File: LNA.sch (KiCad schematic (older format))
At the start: 81 parts, among them CN1 EPS.00.250.NTN, CN2 EPS.00.250.NTN, CN3 EPS.00.250.NTN, CN4 EPS.00.250.NTN, J5 TEST_1P, J6 TEST_1P, J7 TEST_1P, J8 TEST_1P, U1 AD8334ACPZ

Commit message: Bug fixed 1
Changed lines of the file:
@@
 $EndComp
 Connection ~ 5700 7300
-Wire Wire Line
-	5700 5400 5700 5500
 $Comp
 L +5V #PWR21
 U 1 1 599B21E3
-P 5650 5450
-F 0 "#PWR21" H 5650 5300 50  0001 C CNN
-F 1 "+5V" H 5650 5590 50  0000 C CNN
-F 2 "" H 5650 5450 50  0001 C CNN
-F 3 "" H 5650 5450 50  0001 C CNN
-	1    5650 5450
-	0    -1   -1   0
-$EndComp
-Connection ~ 5700 5450
+P 5600 5400
+F 0 "#PWR21" H 5600 5250 50  0001 C CNN
+F 1 "+5V" H 5600 5540 50  0000 C CNN
+F 2 "" H 5600 5400 50  0001 C CNN
+F 3 "" H 5600 5400 50  0001 C CNN
+	1    5600 5400
+	0    -1   -1   0
+$EndComp
 $Comp
 L C_Small C1
@@
 $EndComp
 Wire Wire Line
-	5700 5450 5650 5450
-Wire Wire Line
 	4800 5400 4800 5300
 Connection ~ 4800 5300
@@
 Wire Wire Line
 	1700 6100 1650 6100
+$Comp
+L GNDA #PWR?
+U 1 1 5AD964B4
+P 5550 5500
+F 0 "#PWR?" H 5550 5250 50  0001 C CNN
+F 1 "GNDA" H 5550 5350 50  0000 C CNN
+F 2 "" H 5550 5500 50  0001 C CNN
+F 3 "" H 5550 5500 50  0001 C CNN
+	1    5550 5500
+	1    0    0    -1
+$EndComp
+Wire Wire Line
+	5700 5400 5600 5400
+Wire Wire Line
+	5700 5500 5550 5500
 $EndSCHEMATC

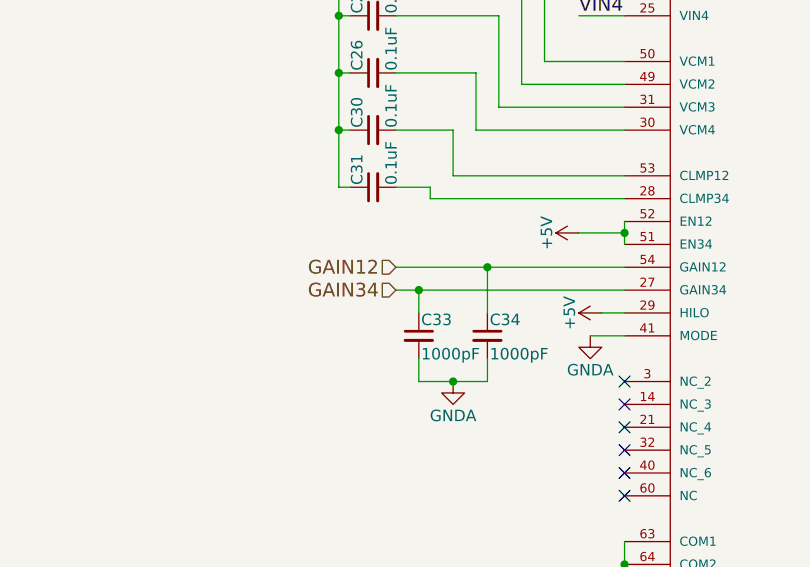
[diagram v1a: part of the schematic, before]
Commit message: add LNA Gain Test Point
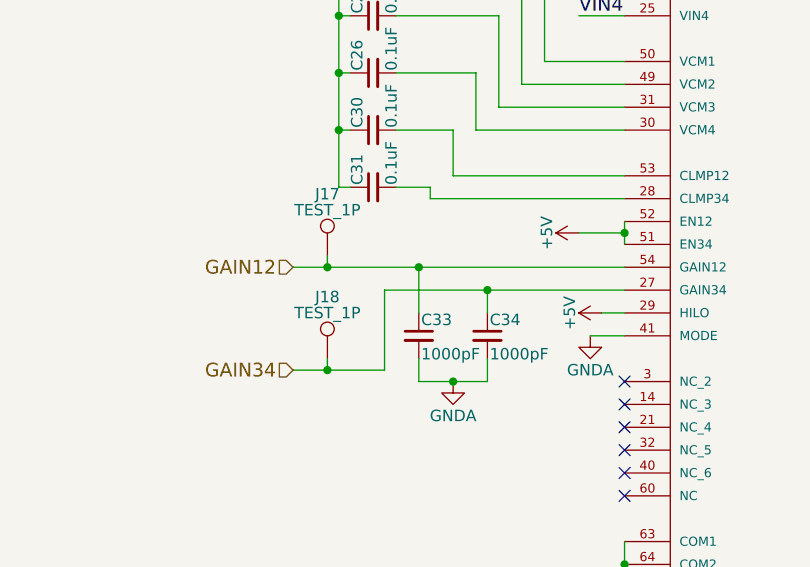
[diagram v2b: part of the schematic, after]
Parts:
- added J17, J18: TEST_1P, symbol TEST_1P
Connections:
- wire segments 229 -> 233

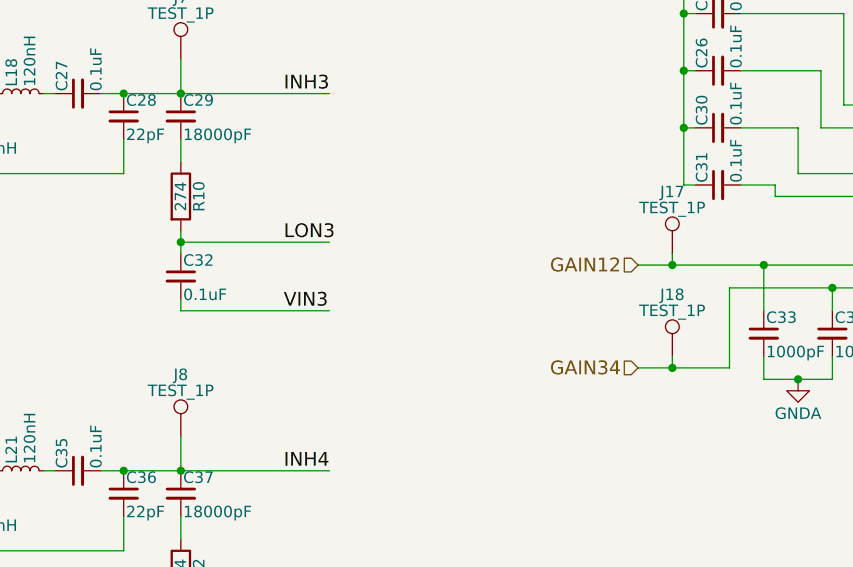
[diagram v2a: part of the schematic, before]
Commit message: Assigned footprint for dimension checking
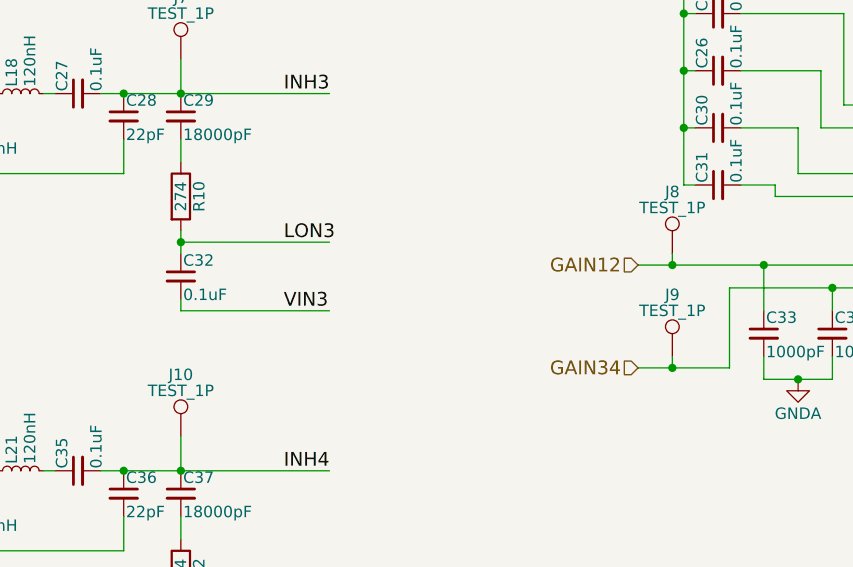
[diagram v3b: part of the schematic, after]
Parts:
- C1, C10, C11, C12, C13, C14, C15, C16, C17, C18, C19, C2, C20, C21, C22, C23, C24, C25, C26, C27, C28, C29, C3, C30, C31, C32, C33, C34, C35, C36, C37, C38, C4, C5, C6, C7, C8, C9: footprint Capacitors_SMD:C_0603 -> Capacitors_SMD:C_0603_HandSoldering
- J10: renamed from J8; footprint Zeabus:1Pin-TP -> Pin_Headers:Pin_Header_Straight_1x01_Pitch2.54mm
- J5, J6, J7: footprint Zeabus:1Pin-TP -> Pin_Headers:Pin_Header_Straight_1x01_Pitch2.54mm
- J8: renamed from J17; footprint (none) -> Pin_Headers:Pin_Header_Straight_1x01_Pitch2.54mm
- J9: renamed from J18; footprint (none) -> Pin_Headers:Pin_Header_Straight_1x01_Pitch2.54mm
- L1, L10, L11, L12, L13, L15, L16, L17, L18, L2, L20, L21, L3, L4, L5, L6, L7, L9: footprint Inductors_SMD:L_0603 -> Inductors_SMD:L_0603_HandSoldering
- R1, R10, R11, R12, R2, R3, R4, R5, R6, R7, R8, R9: footprint Resistors_SMD:R_0603 -> Resistors_SMD:R_0603_HandSoldering
